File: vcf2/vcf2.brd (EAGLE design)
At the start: 58.4 x 107.6 mm, 115 parts, among them IC1 OPA4130U, IC2 OPA4130U, IC3 OPA4130U, IC4 OPA4130U, IC5 OPA4130U, Q7 BC847ASMD

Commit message: vcf2 changes
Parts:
- moved MAXFREQ 64.8 mm to (52.7, 53.3)
- moved C5 0.63 mm to (21.6, 46.4)
- moved R33 0.63 mm to (35.6, 62.9)
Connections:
- new net N$90: R47.2, SV8.4
- net GND: no longer SV7.1, SV8.1
- net N$24: now also SV7.3; no longer SV7.4
- net N$33: now also SV7.2; no longer SV7.3
- net N$50: now also SV8.1; no longer SV8.2
- net N$73: now also SV7.4; no longer R47.2
- net N$79: now also SV8.2; no longer SV8.3
- net N$80: now also SV8.3; no longer SV8.4
- net N$81: now also SV7.1; no longer SV7.2
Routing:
- net N$73: track 0.00 -> 82.5 mm, vias 0 -> 3
- net N$10: track 17.1 -> 39.2 mm, vias 2 -> 3
- net +12V: track 245.0 -> 261.2 mm, vias 14 -> 15
- net N$52: track 100.3 -> 94.6 mm
- net N$35: track 45.5 -> 42.5 mm
- net N$33: track 29.4 -> 26.4 mm, vias 3 -> 2
- net N$27: track 111.8 -> 114.1 mm, vias 5 -> 4
- net N$44: track 72.1 -> 70.0 mm
- net N$22: track 146.9 -> 146.0 mm
- net N$14: track 25.4 -> 24.6 mm
- net N$81: track 56.4 -> 55.7 mm
- net N$39: track 37.9 -> 37.3 mm
- net N$21: track 7.86 -> 7.23 mm
- net N$20: track 24.6 -> 25.3 mm
- net -12V: track 198.9 -> 199.4 mm
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
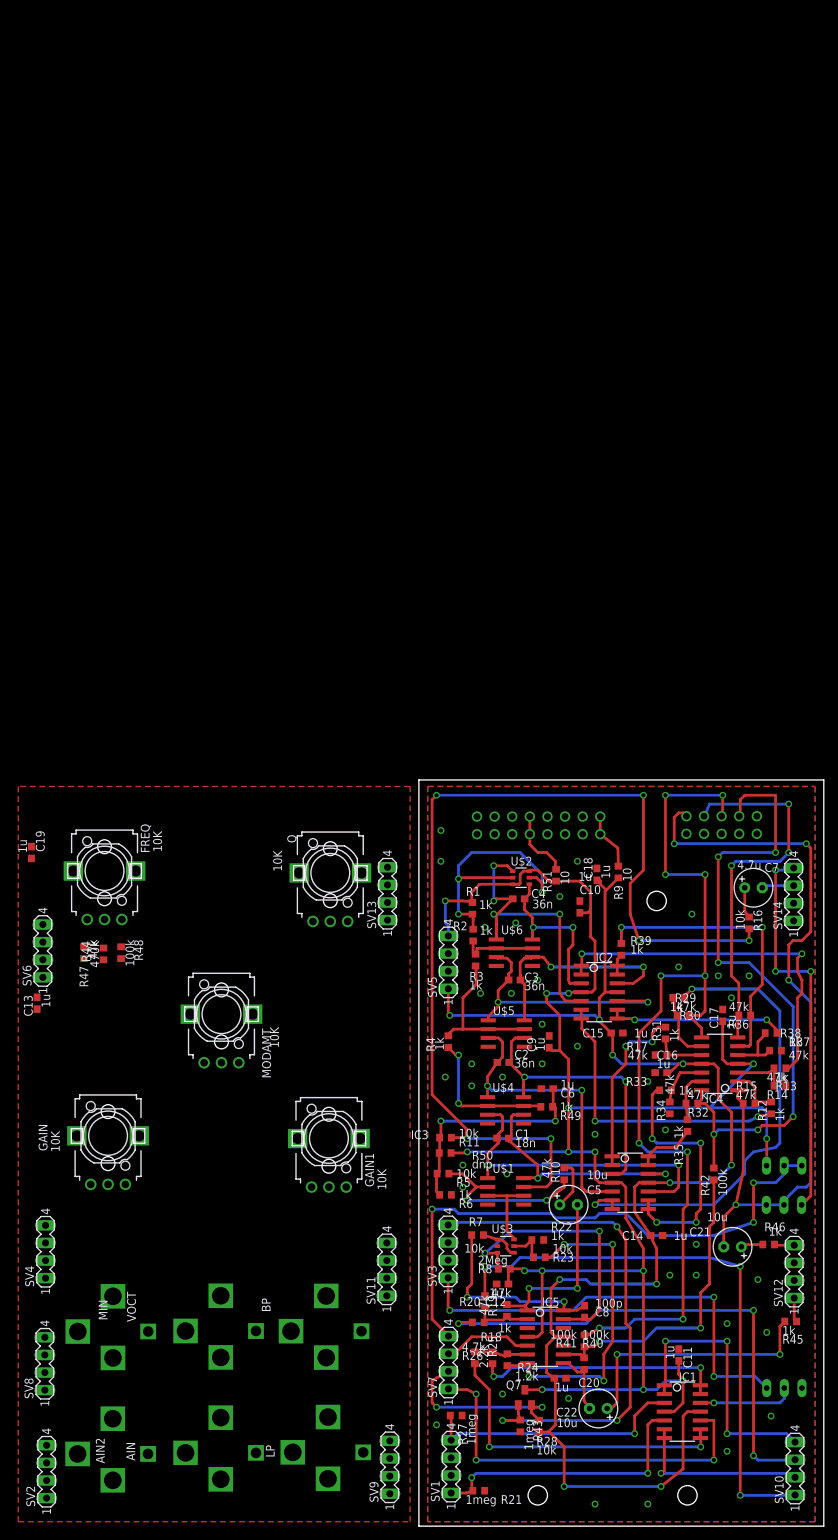
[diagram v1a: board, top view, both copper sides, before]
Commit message: almost finished vcf2 and vca 2nd rev.  Need to verify mechanical dimensions
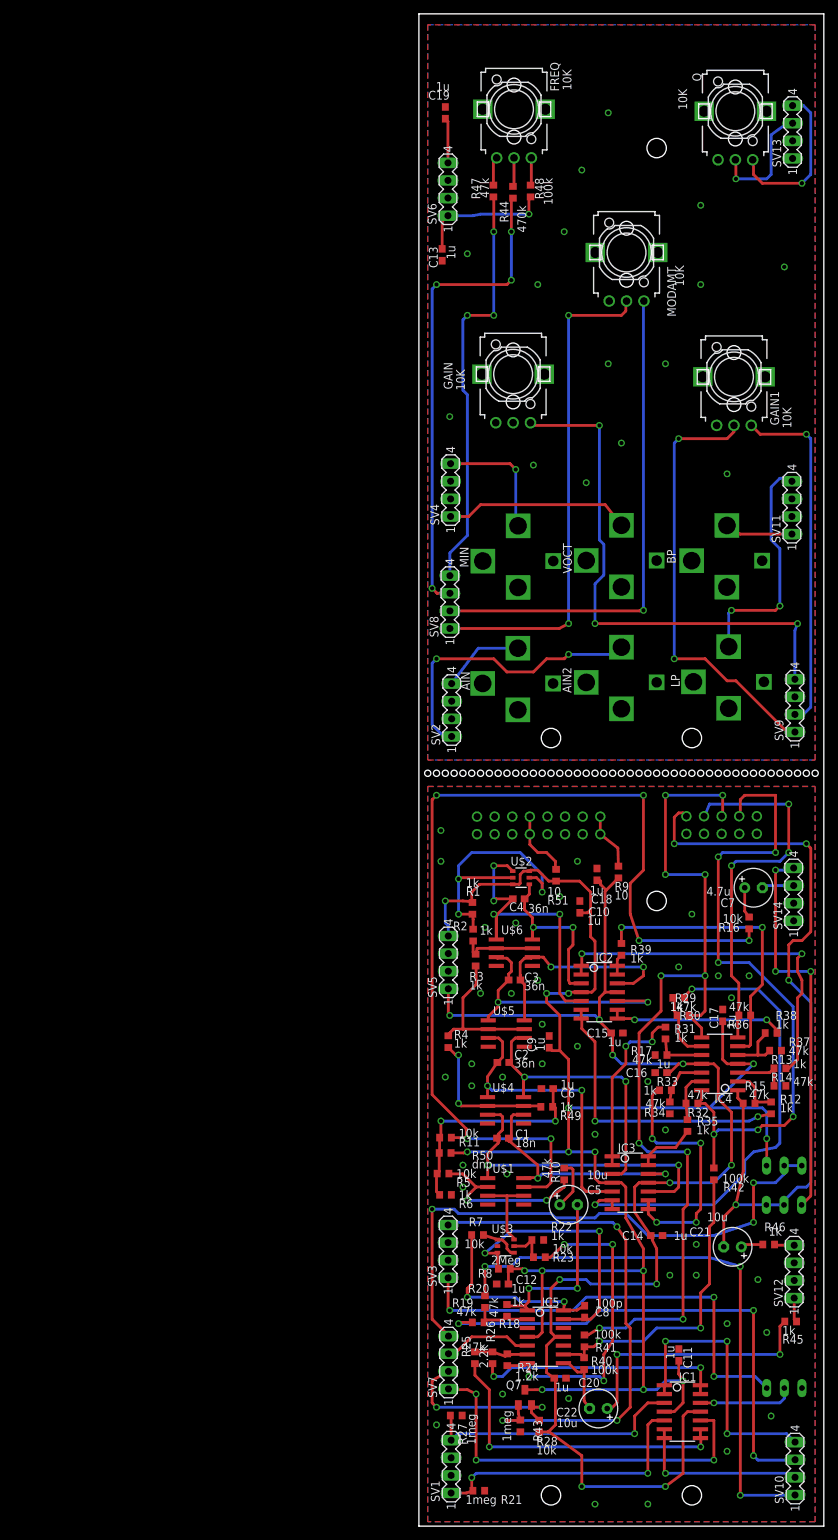
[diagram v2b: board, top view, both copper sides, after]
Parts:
- moved AIN 125.5 mm to (14.3, 121.5)
- moved MIN 125.5 mm to (14.3, 139.2)
- moved AIN2 125.3 mm to (29.2, 121.7)
- moved LP 125.3 mm to (44.7, 121.8)
- moved VPEROCT 125.3 mm to (29.2, 139.3)
- moved BP 125.3 mm to (44.4, 139.2)
- moved R44 124.7 mm to (13.6, 192.4)
- moved R47 124.7 mm to (10.7, 192.6)
- moved R48 124.7 mm to (16.1, 192.6)
- moved FREQ 124.7 mm to (13.7, 204.3)
- moved GAIN 124.4 mm to (13.6, 166.1)
- moved GAIN1 124.4 mm to (45.4, 165.8)
- moved MODAMT 124.4 mm to (29.9, 183.7)
- moved Q 124.4 mm to (45.6, 204.1)
- moved SV4 124.4 mm to (4.57, 149.4)
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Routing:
- net N$85: track 0.00 -> 76.8 mm, vias 0 -> 3
- net N$79: track 0.00 -> 72.5 mm, vias 0 -> 1
- net N$50: track 0.00 -> 71.7 mm, vias 0 -> 2
- net N$80: track 0.00 -> 69.9 mm, vias 0 -> 4
- net N$88: track 0.00 -> 63.1 mm, vias 0 -> 2
- net N$90: track 0.00 -> 60.0 mm, vias 0 -> 3
- net N$57: track 0.00 -> 50.8 mm, vias 0 -> 1
- net N$76: track 0.00 -> 42.7 mm, vias 0 -> 2
- net N$83: track 0.00 -> 34.0 mm, vias 0 -> 2
- net N$78: track 0.00 -> 26.8 mm
- net N$89: track 0.00 -> 23.4 mm, vias 0 -> 1
- net -12V: track 199.4 -> 218.1 mm, vias 10 -> 11
- net N$77: track 0.00 -> 18.0 mm, vias 0 -> 1
- net N$87: track 0.00 -> 17.5 mm, vias 0 -> 1
- net N$75: track 0.00 -> 12.1 mm
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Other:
- board size 58.4 x 107.6 mm -> 58.4 x 218.1 mm

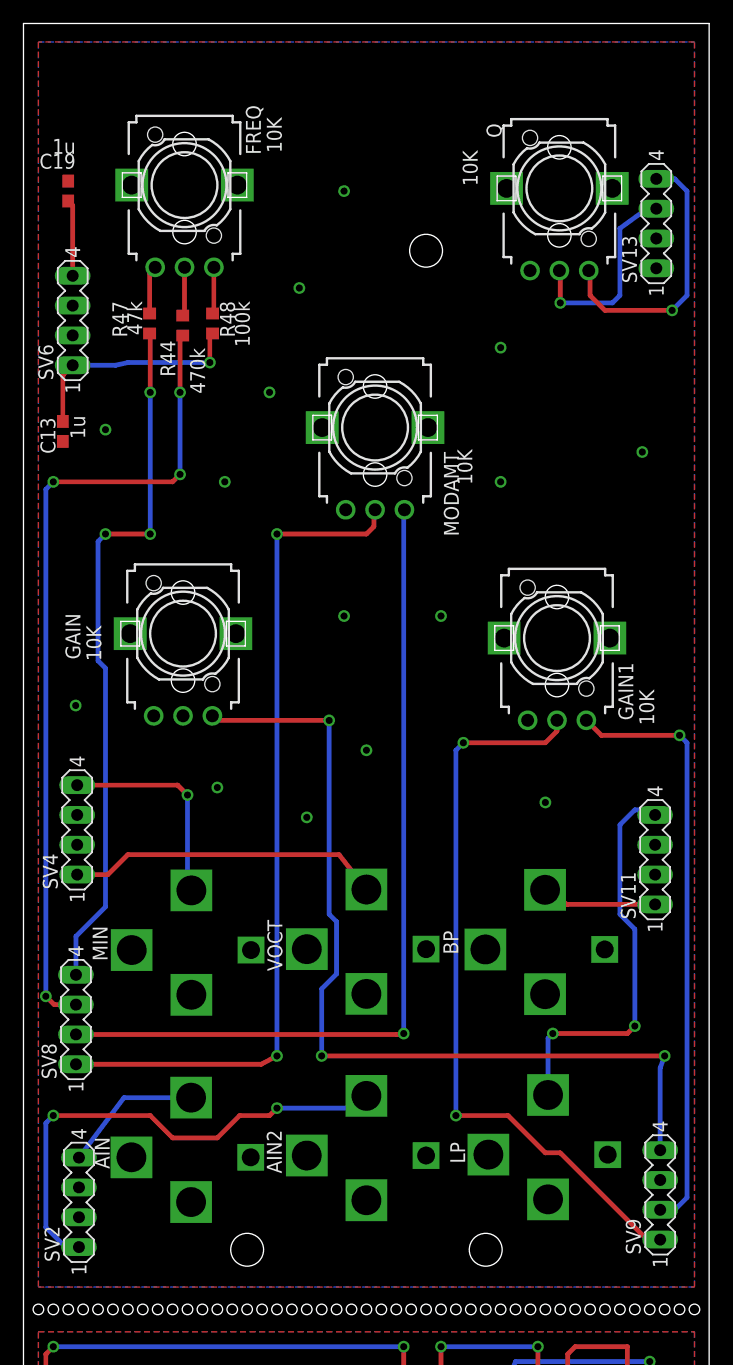
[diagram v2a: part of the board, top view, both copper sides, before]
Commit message: confirmed mechanicals on vcf2
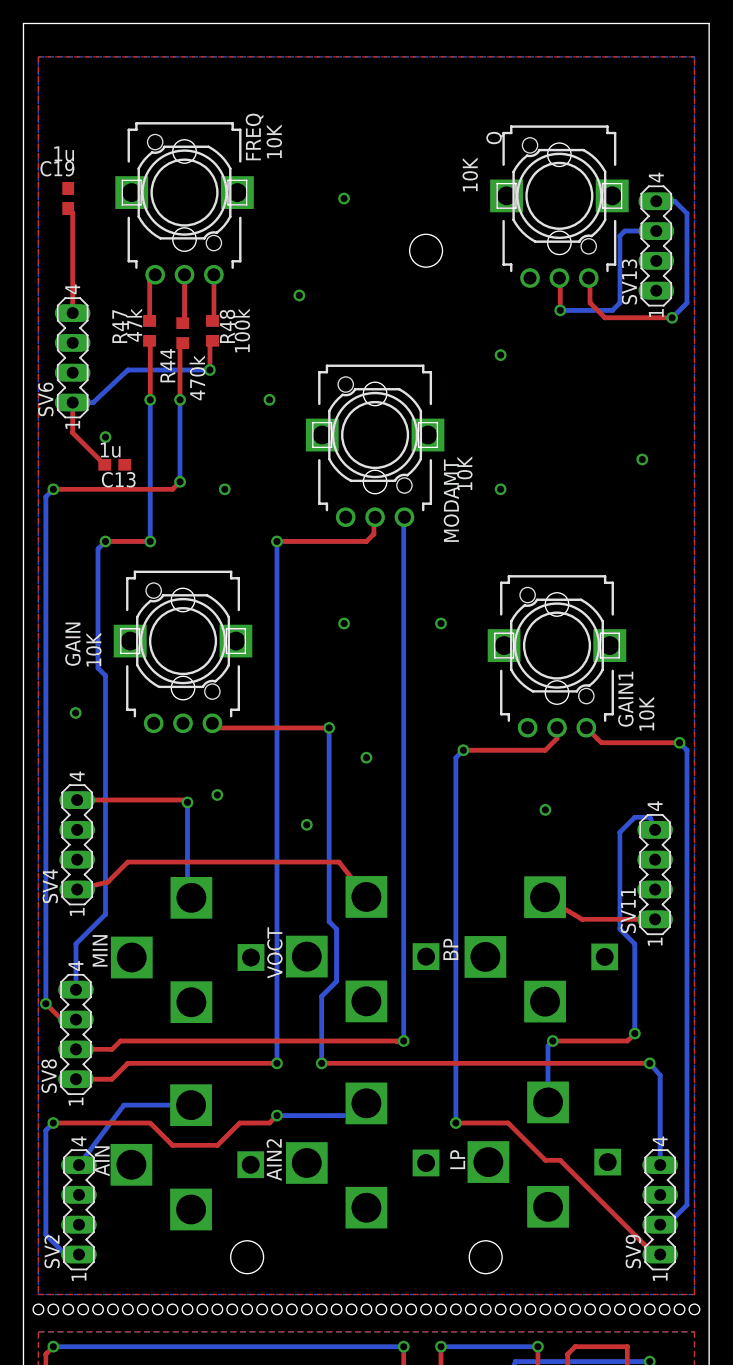
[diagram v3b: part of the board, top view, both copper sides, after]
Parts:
- moved C13 5.26 mm to (7.77, 180.5), turned to 0 degrees
- moved SV6 3.17 mm to (4.19, 189.6)
- moved SV13 1.91 mm to (53.9, 199.2)
- moved SV11 1.27 mm to (53.8, 145.6)
- moved SV4 1.27 mm to (4.57, 148.2)
- moved SV9 1.27 mm to (54.2, 117.1)
- moved SV8 1.27 mm to (4.47, 132.0)
- moved C19 0.64 mm to (3.81, 203.2)
- moved MIN 0.64 mm to (14.3, 138.6)
- moved MODAMT 0.64 mm to (29.9, 183.1)
- moved Q 0.64 mm to (45.6, 203.4)
- moved R44 0.64 mm to (13.6, 191.7)
- moved VPEROCT 0.64 mm to (29.2, 138.6)
- moved AIN 0.64 mm to (14.3, 120.9)
- moved AIN2 0.64 mm to (29.2, 121.1)
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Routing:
- net +12V: track 267.7 -> 270.3 mm
- net -12V: track 218.1 -> 220.5 mm
- net N$89: track 23.4 -> 22.1 mm
- net N$79: track 72.5 -> 73.4 mm
- net N$90: track 60.0 -> 60.7 mm
- net N$83: track 34.0 -> 34.6 mm

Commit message: made gerbers for vcf2
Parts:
- moved GAIN 0.64 mm to (13.6, 164.9)
- moved BP 0.64 mm to (45.1, 138.6)
- moved AIN 0.63 mm to (14.9, 120.9)
- moved MIN 0.63 mm to (14.9, 138.6)
- moved AIN2 0.63 mm to (29.8, 121.1)
- moved LP 0.63 mm to (45.3, 121.1)
- moved VPEROCT 0.63 mm to (29.8, 138.6)
- moved FREQ 0.63 mm to (13.7, 203.1)
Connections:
- net N$86: now also GAIN.2
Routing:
- net N$86: track 0.00 -> 75.9 mm
- net N$88: track 63.3 -> 65.6 mm
- net N$75: track 12.1 -> 12.7 mm
- net N$83: track 34.6 -> 33.9 mm
- net N$66: track 3.98 -> 3.35 mm
- net N$65: track 4.18 -> 3.54 mm
- net N$82: track 9.89 -> 9.36 mm
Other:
- board size 58.4 x 218.1 mm -> 58.4 x 216.8 mm

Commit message: progress..
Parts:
- R19, R20: value 47k -> 22k
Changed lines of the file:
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@@
 <attribute name="VALUE" x="13.335" y="31.75" size="1.27" layer="21" font="vector" ratio="15"/>
 </element>
-<element name="R19" library="dan" package="R0603" value="47k" x="8.5598" y="29.3878" smashed="yes">
+<element name="R19" library="dan" package="R0603" value="22k" x="8.5598" y="29.3878" smashed="yes">
 <attribute name="NAME" x="4.7752" y="31.5722" size="1.27" layer="21" font="vector" ratio="15"/>
 <attribute name="VALUE" x="5.4102" y="30.3022" size="1.27" layer="21" font="vector" ratio="15"/>
@@
 <attribute name="VALUE" x="9.9568" y="83.6676" size="1.27" layer="21" font="vector" ratio="15" rot="R90"/>
 </element>
-<element name="R20" library="dan" package="R0603" value="47k" x="9.525" y="32.385" smashed="yes" rot="R270">
+<element name="R20" library="dan" package="R0603" value="22k" x="9.525" y="32.385" smashed="yes" rot="R270">
 <attribute name="NAME" x="10.16" y="34.925" size="1.27" layer="21" font="vector" ratio="15" rot="R180"/>
-<attribute name="VALUE" x="10.16" y="33.02" size="1.27" layer="21" font="vector" ratio="15" rot="R270"/>
+<attribute name="VALUE" x="10.16" y="33.655" size="1.27" layer="21" font="vector" ratio="15" rot="R270"/>
 </element>
 <element name="GAIN" library="dan" package="EVUFXJ" value="10K" x="13.589" y="164.8714" smashed="yes">
